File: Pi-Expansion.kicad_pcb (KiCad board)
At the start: 2 copper layers, 56 x 65 mm, 130 parts, among them J1 RPi_GPIO, J2 MMCX_H, J3 PINHEADER_2X2_SMD, J4 PINHEADER_2X2_SMD, P1 BATT, U1 A2200-A, U2 Racom R-78B5.0-1.5L

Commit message: Nudged silkscreen for @tomgc96
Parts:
- moved svg2mod 3.40 mm to (114.0, 98.8)
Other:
- board text added: "abersailbot.github.io"
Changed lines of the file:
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@@
     (links 90)
     (no_connects 2)
-    (area 67.5 56.852029 137.75 144.700001)
+    (area 67.819999 72.349999 124.320001 137.850001)
     (thickness 1.6)
-    (drawings 25)
+    (drawings 26)
     (tracks 363)
     (zones 0)
@@
   (page A4)
   (layers
-    (0 F.Cu signal)
-    (31 B.Cu power)
+    (0 F.Cu signal hide)
+    (31 B.Cu power hide)
     (32 B.Adhes user)
     (33 F.Adhes user)
     (34 B.Paste user)
     (35 F.Paste user)
-    (36 B.SilkS user hide)
+    (36 B.SilkS user)
     (37 F.SilkS user)
     (38 B.Mask user)
@@
   )
   (module Sailbot_Custom:Sailbot_Logo (layer F.Cu)
-    (at 115 95.5 90)
+    (at 114 98.75 90)
     (fp_text reference svg2mod (at 0 -6.914931 90) (layer F.SilkS) hide
       (effects (font (thickness 0.3048)))
@@
       (net 1 +3V3))
   )
+  (gr_text abersailbot.github.io (at 118.75 95 90) (layer F.Cu)
+    (effects (font (size 1.5 1.5) (thickness 0.3)))
+  )
   (gr_text 2.2K (at 77.5 121.5) (layer F.SilkS)
     (effects (font (size 1 1) (thickness 0.25)))
@@
     (effects (font (size 1 1) (thickness 0.2)))
   )
-  (gr_text "V1.2.2 'Captain H. Morgan' " (at 108.5 88.5 90) (layer F.SilkS)
+  (gr_text "V1.2.2 'Captain H. Morgan' " (at 108.25 90.5 90) (layer F.SilkS)
     (effects (font (size 1.5 1.5) (thickness 0.3)))
   )
@@
     (effects (font (size 1 1) (thickness 0.25)))
   )
-  (gr_text 2.2K (at 112.8 106.9) (layer F.SilkS)
+  (gr_text 2.2K (at 110.5 108.5) (layer F.SilkS)
     (effects (font (size 1 1) (thickness 0.25)))
   )
@@
   (gr_arc (start 71.57 76.1) (end 68.07 76.1) (angle 90) (layer Edge.Cuts) (width 0.5))
   (gr_arc (start 71.57 134.1) (end 71.57 137.6) (angle 90) (layer Edge.Cuts) (width 0.5))
-  (segment (start 81.89 105.5) (end 77.22 105.5) (width 0.5) (layer F.Cu) (net 1) (status 400000))
+  (segment (start 81.89 105.5) (end 77.22 105.5) (width 0.5) (layer F.Cu) (net 1))
   (segment (start 77.22 105.5) (end 73.81 108.91) (width 0.5) (layer F.Cu) (net 1))
-  (segment (start 73.81 108.91) (end 72.84 108.91) (width 0.5) (layer F.Cu) (net 1) (status 800000))
-  (segment (start 72.84 108.91) (end 73 108.75) (width 0.5) (layer F.Cu) (net 1) (status C00000))
+  (segment (start 73.81 108.91) (end 72.84 108.91) (width 0.5) (layer F.Cu) (net 1))
+  (segment (start 72.84 108.91) (end 73 108.75) (width 0.5) (layer F.Cu) (net 1))
   (segment (start 104.75 105.5) (end 102.21 105.5) (width 0.5) (layer B.Cu) (net 1) (status 30))
   (segment (start 102.21 105.5) (end 99.67 105.5) (width 0.5) (layer B.Cu) (net 1) (status 30))

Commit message: moved url to silkscreen and updated it for .co.uk address
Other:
- board text added: "abersailbot.co.uk"
- board text removed: "abersailbot.github.io"
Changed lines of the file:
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@@
   (page A4)
   (layers
-    (0 F.Cu signal hide)
+    (0 F.Cu signal)
     (31 B.Cu power hide)
     (32 B.Adhes user)
@@
       (net 1 +3V3))
   )
-  (gr_text abersailbot.github.io (at 118.75 95 90) (layer F.Cu)
+  (gr_text abersailbot.co.uk (at 119 97 90) (layer F.SilkS)
     (effects (font (size 1.5 1.5) (thickness 0.3)))
   )

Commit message: Moved led vias and traces to clear around silkscreen.
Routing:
- net Net-(LED5-PadK): track 17.3 -> 19.8 mm
- net PI_LED_4: track 30.4 -> 31.5 mm
- net PI_LED_3: track 27.4 -> 28.4 mm
- net PI_LED_2: track 23.6 -> 24.6 mm
- net Net-(J1-Pad3): track 23.1 -> 24.0 mm

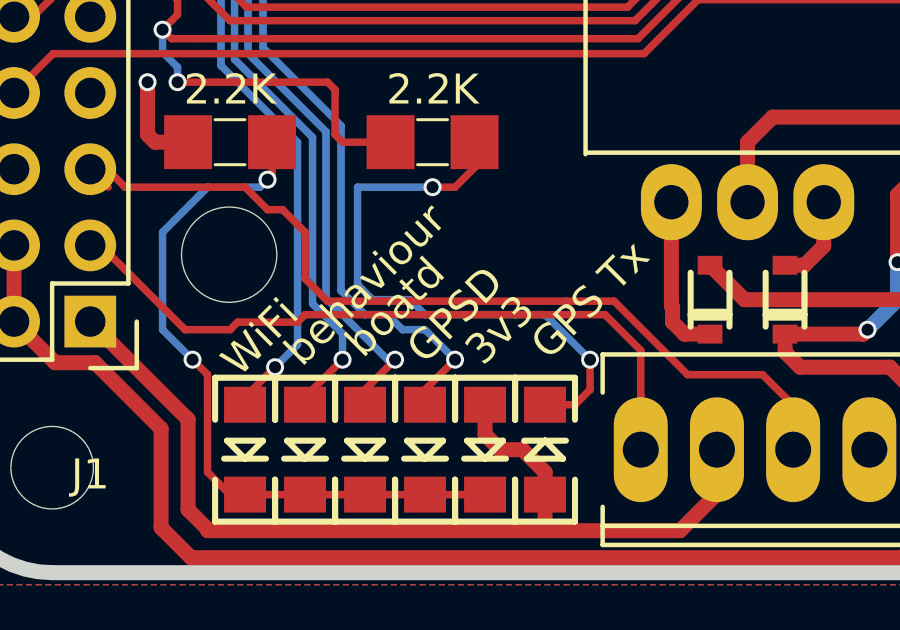
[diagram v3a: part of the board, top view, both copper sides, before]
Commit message: de-capitalised gpsd
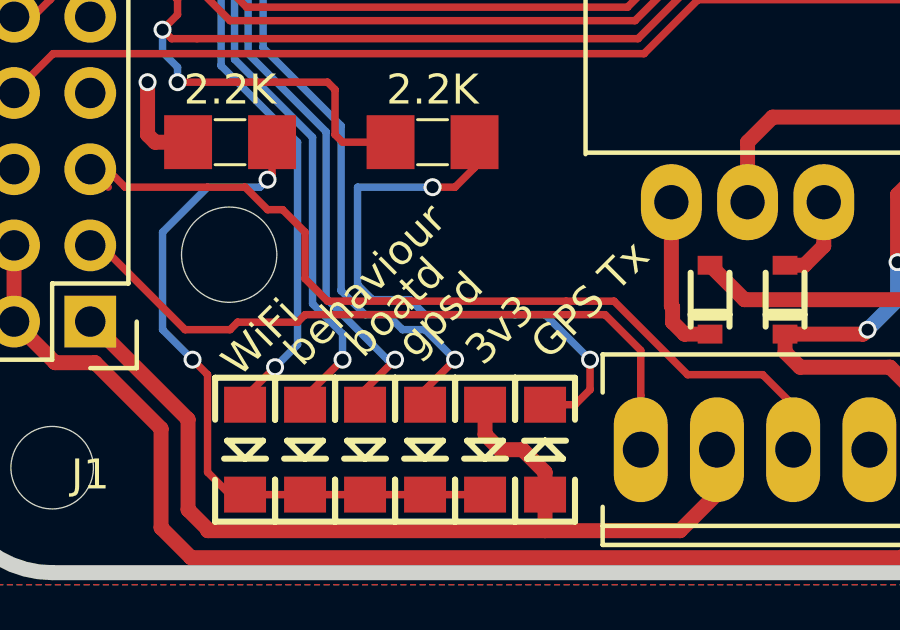
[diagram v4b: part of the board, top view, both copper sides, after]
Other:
- board text added: "gpsd"
- board text removed: "GPSD"
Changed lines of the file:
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@@
     (arrow2b (pts (xy 129.75 72.25) (xy 130.336421 73.376504)))
   )
-  (gr_text GPSD (at 85 129 45) (layer F.SilkS)
+  (gr_text gpsd (at 84.5 129 45) (layer F.SilkS)
     (effects (font (size 1 1) (thickness 0.2)))
   )
